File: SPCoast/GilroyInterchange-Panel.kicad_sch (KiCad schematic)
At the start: 17 parts, among them U6023 0x22, U6024 0x23

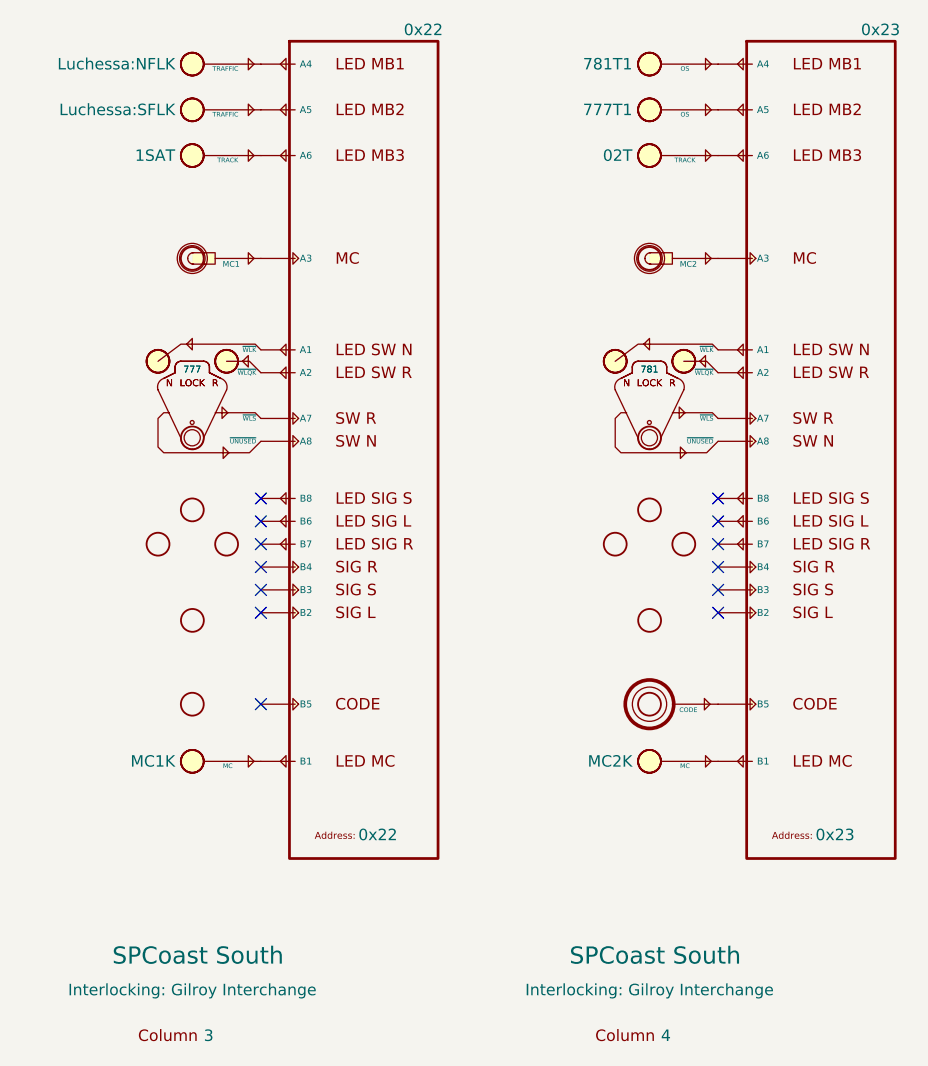
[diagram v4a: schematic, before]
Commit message: feat(kicad): deployment cases: Caltrain on a CMRInet node, Gilroy Interchange JMRI turnouts over MQTT
Gilroy Caltrain: field I/O drawn as per-bit CMRInet drivers (Driver-CMRI-IB/OB,
UA 30, 14 in / 20 out) with named devices for 3 switches, 5 track circuits and
7 heads (four encoder-wired, three lamp-wired). No processor is named: every
chip is on the hosted CMRInet bus, so the field unit runs on that bus's host.

Gilroy Interchange: proof of concept for JMRI turnouts and sensors over MQTT
(Driver-JMRI-Turnout, -Turnout-Feedback, -Sensor-Feedback) on switches 777
and 781. Known: the 777 drivers carry Address 771 (typo, fixed by the
follow-up rewrite); the JMRI symbols fail lint_symbol_fields (Pin.D names no
pin, Topic/States casing), also fixed by the rewrite.

Libraries: Railroad-HardwareIO gains Driver-CMRI-IB/OB and the four JMRI
drivers; Railroad-Field's Device-Head-CPL pins renumbered top down (G, Y, R).
Nine other sheets were re-saved by KiCad with property placements only.

Verified:
- kicad-cli ERC: 0 violations, whole project
- every Caltrain and Gilroy Interchange device binds; no duplicate CMRI bits
- netlist_diff vs post-sync.net: only additions on the two sheets (49 parts,
  34 nets, 68 nodes), nothing lost or changed elsewhere
- library-owned field drift on the new instances: 0

Co-Authored-By: Claude Fable 5.1 <noreply@anthropic.com>
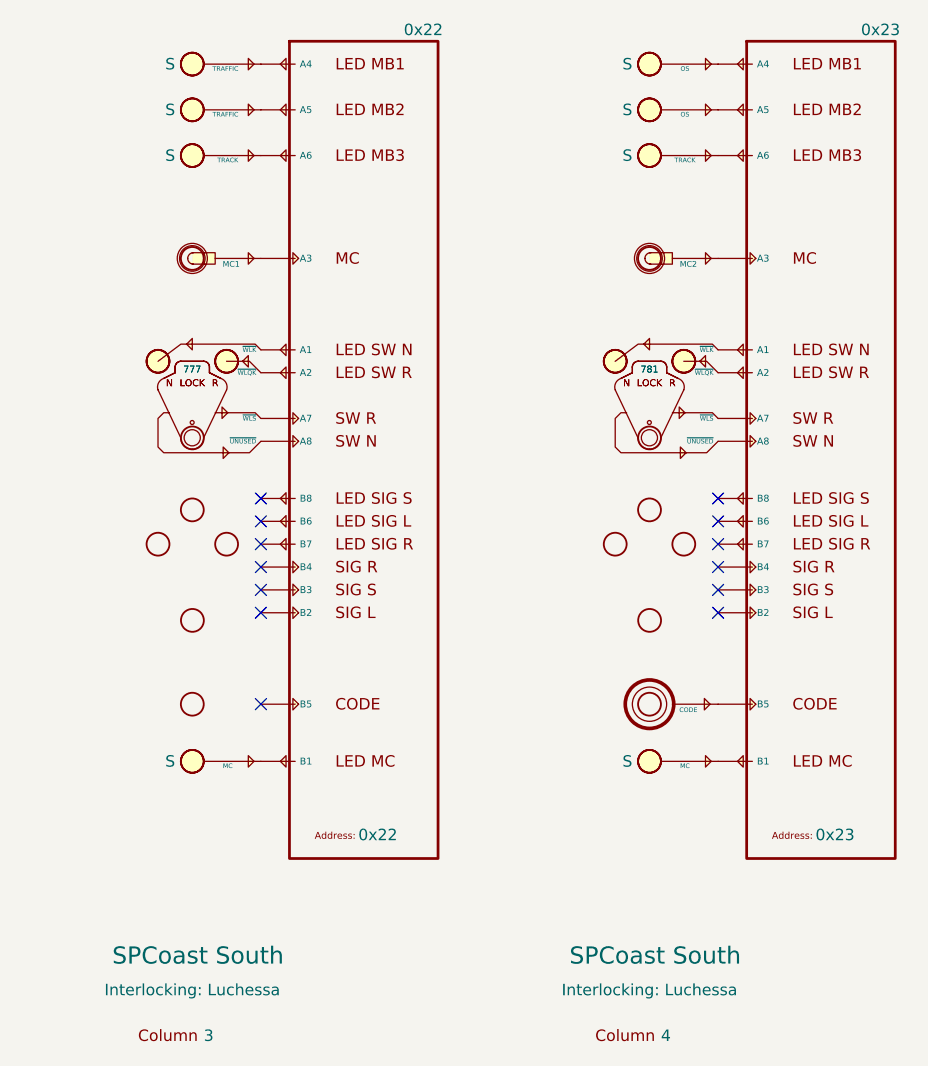
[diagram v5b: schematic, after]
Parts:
- COL6023, COL6024: Interlocking Gilroy Interchange -> Luchessa
- LMP6031: IndicationToken Luchessa:NFLK -> S
- LMP6032: IndicationToken Luchessa:SFLK -> S
- LMP6033: IndicationToken 1SAT -> S
- LMP6041: IndicationToken 781T1 -> S
- LMP6042: IndicationToken 777T1 -> S
- LMP6043: IndicationToken 02T -> S
- MCK6003: IndicationToken MC1K -> S
- MCK6004: IndicationToken MC2K -> S
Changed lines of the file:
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@@
 			)
 		)
-		(property "IndicationToken" "781T1"
+		(property "IndicationToken" "S"
 			(at 128.905 26.67 0)
 			(show_name no)
@@
 			)
 		)
-		(property "IndicationToken" "Luchessa:SFLK"
+		(property "IndicationToken" "S"
 			(at 78.105 31.75 0)
 			(show_name no)
@@
 			)
 		)
-		(property "IndicationToken" "1SAT"
+		(property "IndicationToken" "S"
 			(at 78.105 36.83 0)
 			(show_name no)
@@
 			)
 		)
-		(property "IndicationToken" "MC2K"
+		(property "IndicationToken" "S"
 			(at 128.905 104.14 0)
 			(show_name no)
@@
 			)
 		)
-		(property "ki_locked" ""
-			(at 130.81 63.5 0)
-			(hide yes)
-			(show_name no)
-			(do_not_autoplace no)
-			(effects
-				(font
-					(size 1.27 1.27)
-				)
-			)
-		)
 		(pin "1"
 		)
@@
 			)
 		)
-		(property "ki_locked" ""
-			(at 80.01 63.5 0)
-			(hide yes)
-			(show_name no)
-			(do_not_autoplace no)
-			(effects
-				(font
-					(size 1.27 1.27)
-				)
-			)
-		)
 		(pin "1"
 		)
@@
 			)
 		)
-		(property "IndicationToken" "02T"
+		(property "IndicationToken" "S"
 			(at 128.905 36.83 0)
 			(show_name no)
@@
 			)
 		)
-		(property "ki_locked" ""
-			(at 80.01 63.5 0)
-			(hide yes)
-			(show_name no)
-			(do_not_autoplace no)
-			(effects
-				(font
-					(size 1.27 1.27)
-				)
-			)
-		)
 		(pin "4"
 		)
@@
 			)
 		)
-		(property "Interlocking" "Gilroy Interchange"
+		(property "Interlocking" "Luchessa"
 			(at 130.81 129.54 0)
 			(show_name yes)
@@
 			)
 		)
-		(property "IndicationToken" "Luchessa:NFLK"
+		(property "IndicationToken" "S"
 			(at 78.105 26.67 0)
 			(show_name no)
@@
 			)
 		)
-		(property "Interlocking" "Gilroy Interchange"
+		(property "Interlocking" "Luchessa"
 			(at 80.01 129.54 0)
 			(show_name yes)
@@
 			)
 		)
-		(property "IndicationToken" "MC1K"
+		(property "IndicationToken" "S"
 			(at 78.105 104.14 0)
 			(show_name no)
@@
 			)
 		)
-		(property "ki_locked" ""
-			(at 130.81 63.5 0)
-			(hide yes)
-			(show_name no)
-			(do_not_autoplace no)
-			(effects
-				(font
-					(size 1.27 1.27)
-				)
-			)
-		)
 		(pin "4"
 		)
@@
 			)
 		)
-		(property "IndicationToken" "777T1"
+		(property "IndicationToken" "S"
 			(at 128.905 31.75 0)
 			(show_name no)

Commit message: refactor(kicad): mast anchors with explicit indication-to-aspect casts; restore fields KiCad reset
Second pass after the cast chains (b4c58d3), decided 2026-10-17: the per-head
anchors Head-CPL/CL/Semaphore were the mast's indication table collapsed into
a symbol. The chain is now

    [Mast 774NAB] -indication- [Cast-Aspect-CPL unit B] -aspect- [Cast-Encoder-CPL] -bits- [chip]

Cast-Aspect-CPL/CL/Semaphore are multi-unit casts, one unit per head letter
(A..E), so placing unit B beside mast 774N is head 774NB with nothing typed;
the reader derives every head name from mast plus unit. Style's home is the
aspect cast. The project ERC now ignores missing_unit and missing_input_pin,
since an aspect cast places only the units its mast has.

CMRI bits: Address is the node (the chip every bit folds into, as for every
other driver), Bit is the bit, UA = ${Address} is a display echo, Value =
UA${Address}.IN.${Bit}.

Restore (SPCoast/edits/2026-10-17-restore-reset-fields.py): the owner's last
KiCad save before 857cae2 ran "update symbols from library" with field reset,
putting library defaults into per-instance fields on nine sheets: every
PanelLamp IndicationToken ("S"), PanelColumn Interlocking ("Luchessa"),
Luchessa encoding Station ("Panel"), Sargent Exp2 PCA9685-PWM 0x27 -> 0x20
(colliding with Exp3), and the 34 Caltrain bit numbers. All 98 values are
restored from the last good netlist export, embedded in the script.

Scripts: SPCoast/edits/2026-10-17-mast-chain.py (second pass; reuses the
first pass's helpers), 2026-10-17-restore-reset-fields.py. __pycache__/
added to .gitignore.

Verified:
- post-restore netlist vs the last good export: no field differs except on
  the anchors the first pass replaced and the intended JMRI blanks
- lint_symbol_fields: 93 symbols, 0 errors (per-unit cast rule)
- kicad-cli ERC: 0 violations; netlist export without warnings
- gate vs post-restore: nets not touching an anchor identical; all 11 aspect
  nets re-sourced from a Cast-Aspect un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
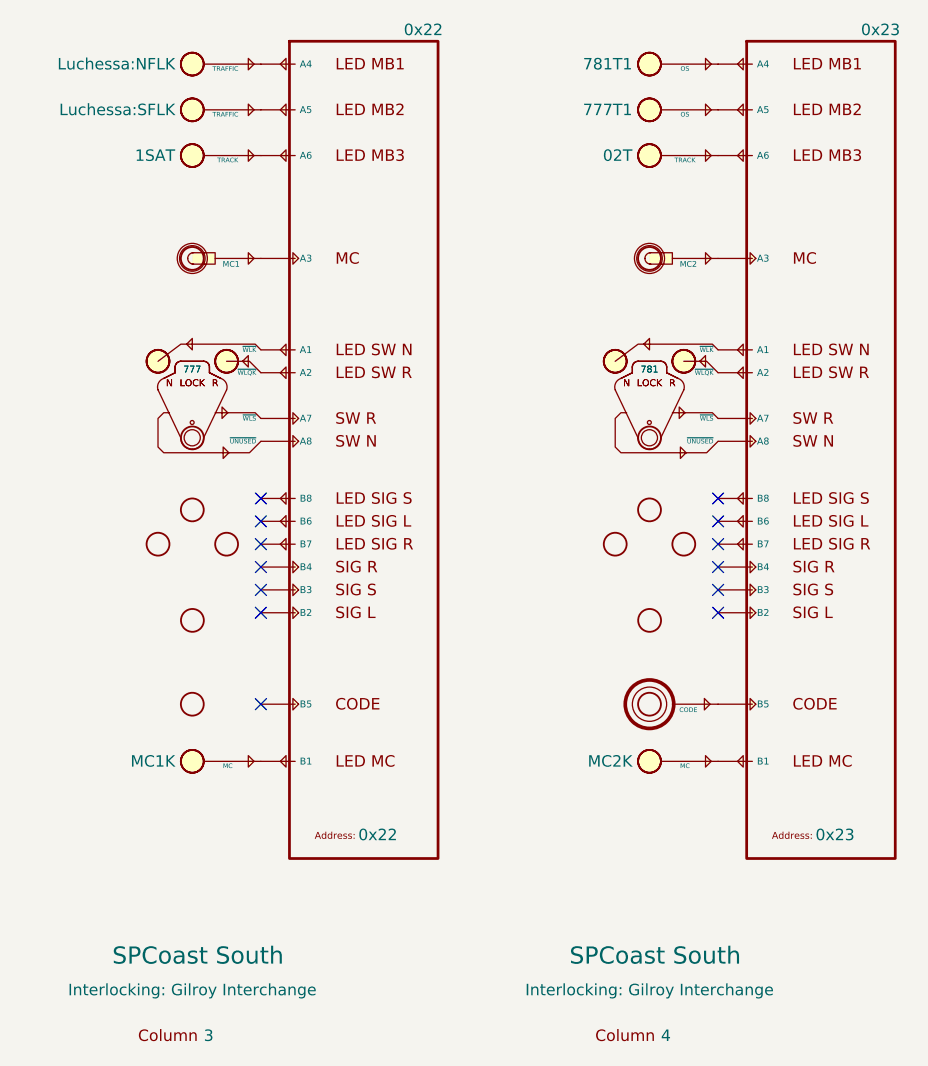
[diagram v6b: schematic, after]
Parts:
- COL6023, COL6024: Interlocking Luchessa -> Gilroy Interchange
- LMP6031: IndicationToken S -> Luchessa:NFLK
- LMP6032: IndicationToken S -> Luchessa:SFLK
- LMP6033: IndicationToken S -> 1SAT
- LMP6041: IndicationToken S -> 781T1
- LMP6042: IndicationToken S -> 777T1
- LMP6043: IndicationToken S -> 02T
- MCK6003: IndicationToken S -> MC1K
- MCK6004: IndicationToken S -> MC2K
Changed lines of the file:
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@@
 			)
 		)
-		(property "IndicationToken" "S"
+		(property "IndicationToken" "781T1"
 			(at 128.905 26.67 0)
 			(show_name no)
@@
 			)
 		)
-		(property "IndicationToken" "S"
+		(property "IndicationToken" "Luchessa:SFLK"
 			(at 78.105 31.75 0)
 			(show_name no)
@@
 			)
 		)
-		(property "IndicationToken" "S"
+		(property "IndicationToken" "1SAT"
 			(at 78.105 36.83 0)
 			(show_name no)
@@
 			)
 		)
-		(property "IndicationToken" "S"
+		(property "IndicationToken" "MC2K"
 			(at 128.905 104.14 0)
 			(show_name no)
@@
 			)
 		)
-		(property "IndicationToken" "S"
+		(property "IndicationToken" "02T"
 			(at 128.905 36.83 0)
 			(show_name no)
@@
 			)
 		)
-		(property "Interlocking" "Luchessa"
+		(property "Interlocking" "Gilroy Interchange"
 			(at 130.81 129.54 0)
 			(show_name yes)
@@
 			)
 		)
-		(property "IndicationToken" "S"
+		(property "IndicationToken" "Luchessa:NFLK"
 			(at 78.105 26.67 0)
 			(show_name no)
@@
 			)
 		)
-		(property "Interlocking" "Luchessa"
+		(property "Interlocking" "Gilroy Interchange"
 			(at 80.01 129.54 0)
 			(show_name yes)
@@
 			)
 		)
-		(property "IndicationToken" "S"
+		(property "IndicationToken" "MC1K"
 			(at 78.105 104.14 0)
 			(show_name no)
@@
 			)
 		)
-		(property "IndicationToken" "S"
+		(property "IndicationToken" "777T1"
 			(at 128.905 31.75 0)
 			(show_name no)

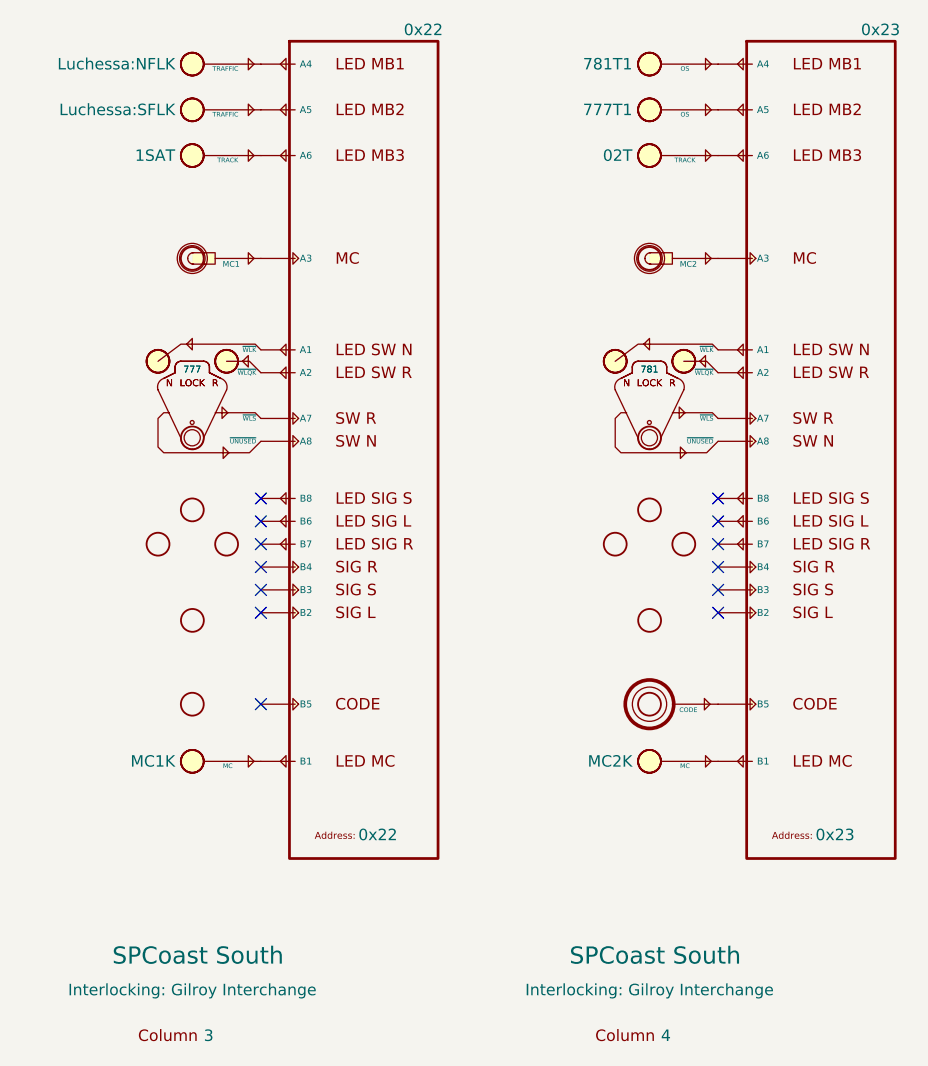
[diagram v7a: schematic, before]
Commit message: chore(kicad): owner edits: GPIO drivers carry Address, Sargent I2C addresses, CMRI body text from fields
Baseline of the owner's saved work before the ADR 0005 scripts:
- Driver-GPIO-Digital and Driver-GPIO-Pixel gain an Address field (the
  board pin); Value renders ${Address}; body text and arrow adjusted.
- Driver-CMRI-IB/OB body text renders UA${Address}.IN/OUT.${Bit} from
  the fields instead of ${VALUE}.
- Sargent, Gilroy Interchange and Luchessa GPIO instances carry Address;
  Sargent Exp2 back at 0x26, Exp3 0x27.
- All sheets resaved by KiCad 10 (reordering), project file
  used_designators cleared by KiCad.

Verified: no lock files; committed as saved, unverified by netlist (the
baseline netlist is exported in the next step).

Co-Authored-By: Claude Fable 5.1 <noreply@anthropic.com>
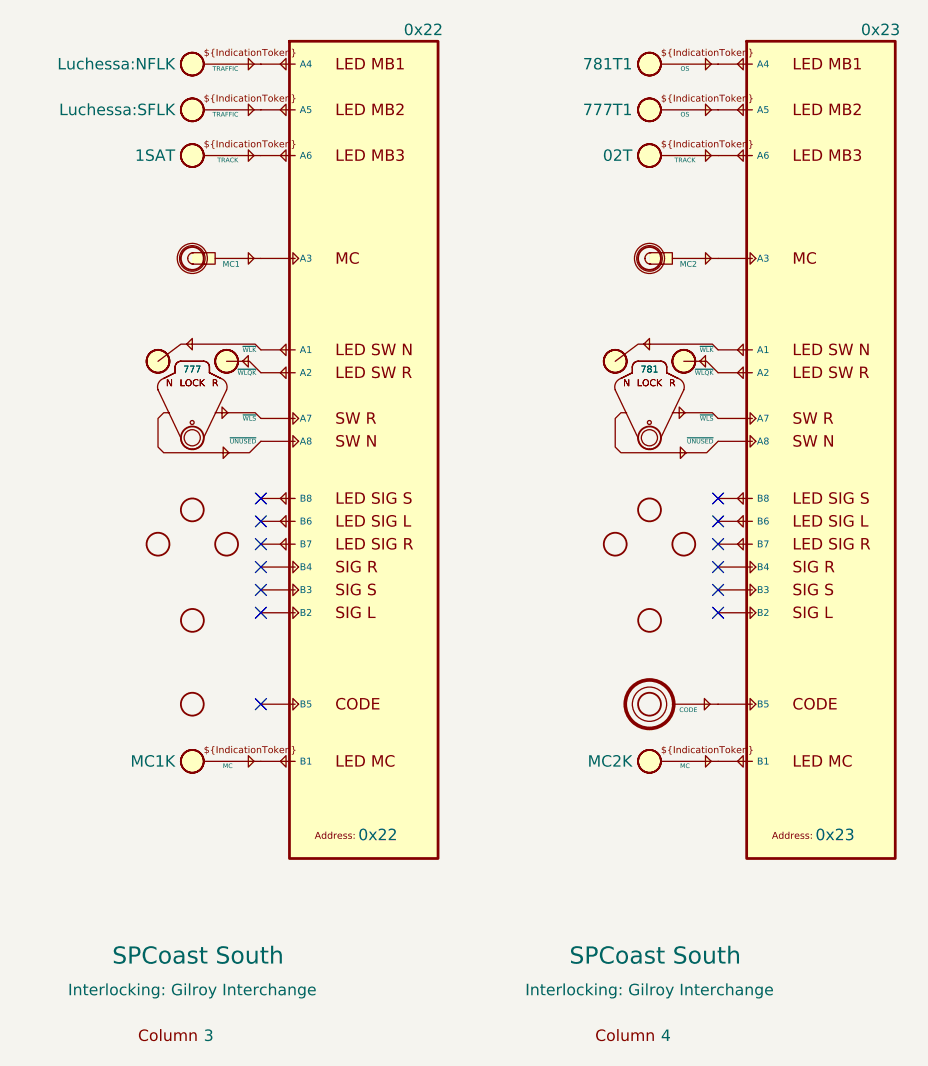
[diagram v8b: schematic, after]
